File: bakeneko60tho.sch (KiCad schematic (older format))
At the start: 14 parts

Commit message: assign footprints
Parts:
- added D1, D10, D11, D12, D13, D14, D15, D16, D17, D18, D19, D2, D20, D21, D22, D23, D24, D25, D26, D27, D28, D29, D3, D30, D31, D32, D33, D34, D35, D36, D37, D38, D39, D4, D40, D41, D42, D43, D44, D45, D46, D47, D48, D49, D5, D50, D51, D52, D53, D54, D55, D56, D57, D58, D59, D6, D60, D61, D62, D63, D64, D65, D66, D67, D68, D69, D7, D70, D71, D72, D8, D9: SOD-123, Diode_SMD:D_SOD-123, symbol Device:D_Small
- added F1: 500mA, Fuse:Fuse_1206_3216Metric, symbol Device:Polyfuse
- added J1: Conn_01x04_Male, Connector_PinHeader_1.00mm:PinHeader_1x04_P1.00mm_Horizontal, symbol Connector:Conn_01x04_Male
- added MX1, MX10, MX11, MX12, MX13, MX14, MX15, MX16, MX17, MX18, MX19, MX2, MX20, MX21, MX22, MX23, MX24, MX25, MX26, MX27, MX28, MX29, MX3, MX30, MX31, MX32, MX33, MX34, MX35, MX36, MX37, MX38, MX39, MX4, MX40, MX41, MX42, MX44, MX45, MX46, MX47, MX48, MX49, MX5, MX50, MX51, MX52, MX53, MX54, MX55, MX57, MX58, MX59, MX6, MX60, MX61, MX62, MX63, MX65, MX66, MX67, MX68, MX69, MX7, MX70, MX71, MX72, MX8, MX9: MX-NoLED, MX_Only:MXOnly-1U-NoLED, symbol MX_Alps_Hybrid:MX-NoLED
- added MX43, MX56: MX-NoLED, MX_Only:MXOnly-2U-NoLED, symbol MX_Alps_Hybrid:MX-NoLED
- added MX64: MX-NoLED, MX_Only:MXOnly-2U-ReversedStabilizers-NoLED, symbol MX_Alps_Hybrid:MX-NoLED
- C1, C2, C3, C4, C5, C6: renamed from C?; footprint (none) -> Capacitor_SMD:C_0805_2012Metric
- C7: renamed from C?; value 0.1uF -> 10uF; footprint (none) -> Capacitor_SMD:C_0805_2012Metric
- R1, R2, R3, R4: renamed from R?; footprint (none) -> Resistor_SMD:R_0805_2012Metric
- Y1: renamed from Y?; footprint (none) -> Crystal:Crystal_SMD_3225-4Pin_3.2x2.5mm
- gave numbers to parts that had none: 2
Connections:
- net +5V: now also F1.1
- net D+: now also J1.3 (Pin_3)
- net D-: now also J1.2 (Pin_2)
- net GND: now also J1.4 (Pin_4)
- net COL12: now reaches U1.10 (PB2)
- net COL12: now also MX13.1 (COL), MX28.1 (COL), MX43.1 (COL), MX70.1 (COL)
- net COL11: now reaches U1.11 (PB3)
- net COL11: now also MX12.1 (COL), MX27.1 (COL), MX42.1 (COL), MX56.1 (COL), MX69.1 (COL)
- net COL7: now reaches U1.12 (PB7)
- net COL7: now also MX23.1 (COL), MX38.1 (COL), MX52.1 (COL), MX65.1 (COL), MX8.1 (COL)
- net COL6: now reaches U1.18 (PD0)
- net COL6: now also MX22.1 (COL), MX37.1 (COL), MX51.1 (COL), MX7.1 (COL)
- net COL5: now reaches U1.19 (PD1)
- net COL5: now also MX21.1 (COL), MX36.1 (COL), MX50.1 (COL), MX6.1 (COL), MX64.1 (COL)
- net COL4: now reaches U1.20 (PD2)
- net COL4: now also MX20.1 (COL), MX35.1 (COL), MX49.1 (COL), MX5.1 (COL), MX63.1 (COL)
- net COL3: now reaches U1.21 (PD3)
- net COL3: now also MX19.1 (COL), MX34.1 (COL), MX4.1 (COL), MX48.1 (COL), MX62.1 (COL)
- net COL2: now reaches U1.26 (PD6)
- net COL2: now also MX18.1 (COL), MX3.1 (COL), MX33.1 (COL), MX47.1 (COL), MX61.1 (COL)
- net COL1: now reaches U1.27 (PD7)
- net COL1: now also MX17.1 (COL), MX2.1 (COL), MX32.1 (COL), MX46.1 (COL), MX60.1 (COL)
- net COL10: now reaches U1.28 (PB4)
- net COL10: now also MX11.1 (COL), MX26.1 (COL), MX41.1 (COL), MX55.1 (COL), MX68.1 (COL)
- net COL9: now reaches U1.29 (PB5)
- net COL9: now also MX10.1 (COL), MX25.1 (COL), MX40.1 (COL), MX54.1 (COL), MX67.1 (COL)
- net COL8: now reaches U1.30 (PB6)
- net COL8: now also MX24.1 (COL), MX39.1 (COL), MX53.1 (COL), MX66.1 (COL), MX9.1 (COL)
- net ROW4: now reaches U1.36 (PF7)
- net ROW4: now also D59.1 (K), D60.1 (K), D61.1 (K), D62.1 (K), D63.1 (K), D64.1 (K), D65.1 (K), D66.1 (K), D67.1 (K), D68.1 (K), D69.1 (K), D70.1 (K), D71.1 (K), D72.1 (K)
- net ROW3: now reaches U1.37 (PF6)
- net ROW3: now also D45.1 (K), D46.1 (K), D47.1 (K), D48.1 (K), D49.1 (K), D50.1 (K), D51.1 (K), D52.1 (K), D53.1 (K), D54.1 (K), D55.1 (K), D56.1 (K), D57.1 (K), D58.1 (K)
- net ROW2: now reaches U1.38 (PF5)
- net ROW2: now also D31.1 (K), D32.1 (K), D33.1 (K), D34.1 (K), D35.1 (K), D36.1 (K), D37.1 (K), D38.1 (K), D39.1 (K), D40.1 (K), D41.1 (K), D42.1 (K), D43.1 (K), D44.1 (K)
- net ROW1: now reaches U1.39 (PF4)
- net ROW1: now also D16.1 (K), D17.1 (K), D18.1 (K), D19.1 (K), D20.1 (K), D21.1 (K), D22.1 (K), D23.1 (K), D24.1 (K), D25.1 (K), D26.1 (K), D27.1 (K), D28.1 (K), D29.1 (K), D30.1 (K)
- net ROW0: now reaches U1.40 (PF1)
- net ROW0: now also D1.1 (K), D10.1 (K), D11.1 (K), D12.1 (K), D13.1 (K), D14.1 (K), D15.1 (K), D2.1 (K), D3.1 (K), D4.1 (K), D5.1 (K), D6.1 (K), D7.1 (K), D8.1 (K), D9.1 (K)
- net COL0: now reaches U1.41 (PF0)
- net COL0: now also MX1.1 (COL), MX16.1 (COL), MX31.1 (COL), MX45.1 (COL), MX59.1 (COL)
- net COL14: now reaches U1.8 (PB0)
- net COL14: now also MX15.1 (COL), MX30.1 (COL), MX44.1 (COL), MX58.1 (COL), MX72.1 (COL)
- net COL13: now reaches U1.9 (PB1)
- net COL13: now also MX14.1 (COL), MX29.1 (COL), MX57.1 (COL), MX71.1 (COL)
- new net: D36.2 (A), MX36.2 (ROW)
- new net: D37.2 (A), MX37.2 (ROW)
- new net: D38.2 (A), MX38.2 (ROW)
- new net: D39.2 (A), MX39.2 (ROW)
- new net: D40.2 (A), MX40.2 (ROW)
- new net: D41.2 (A), MX41.2 (ROW)
- new net: D42.2 (A), MX42.2 (ROW)
- new net: D43.2 (A), MX43.2 (ROW)
- new net: D44.2 (A), MX44.2 (ROW)
- new net: D31.2 (A), MX31.2 (ROW)
- new net: D32.2 (A), MX32.2 (ROW)
- new net: D33.2 (A), MX33.2 (ROW)
- new net: D34.2 (A), MX34.2 (ROW)
- new net: D35.2 (A), MX35.2 (ROW)
- new net: D50.2 (A), MX50.2 (ROW)
- new net: D51.2 (A), MX51.2 (ROW)
- new net: D52.2 (A), MX52.2 (ROW)
- new net: D53.2 (A), MX53.2 (ROW)
- new net: D54.2 (A), MX54.2 (ROW)
- new net: D55.2 (A), MX55.2 (ROW)
- new net: D56.2 (A), MX56.2 (ROW)
- new net: D57.2 (A), MX57.2 (ROW)
- new net: D58.2 (A), MX58.2 (ROW)
- new net: D45.2 (A), MX45.2 (ROW)
- new net: D46.2 (A), MX46.2 (ROW)
- new net: D47.2 (A), MX47.2 (ROW)
- new net: D48.2 (A), MX48.2 (ROW)
- new net: D49.2 (A), MX49.2 (ROW)
- new net: D64.2 (A), MX64.2 (ROW)
- new net: D65.2 (A), MX65.2 (ROW)
- new net: D66.2 (A), MX66.2 (ROW)
- new net: D67.2 (A), MX67.2 (ROW)
- new net: D68.2 (A), MX68.2 (ROW)
- new net: D69.2 (A), MX69.2 (ROW)
- new net: D70.2 (A), MX70.2 (ROW)
- new net: D71.2 (A), MX71.2 (ROW)
- new net: D72.2 (A), MX72.2 (ROW)
- new net: D59.2 (A), MX59.2 (ROW)
- new net: D60.2 (A), MX60.2 (ROW)
- new net: D61.2 (A), MX61.2 (ROW)
- new net: D62.2 (A), MX62.2 (ROW)
- new net: D63.2 (A), MX63.2 (ROW)
- new net: D6.2 (A), MX6.2 (ROW)
- new net: D7.2 (A), MX7.2 (ROW)
- new net: D8.2 (A), MX8.2 (ROW)
- new net: D9.2 (A), MX9.2 (ROW)
- new net: D10.2 (A), MX10.2 (ROW)
- new net: D11.2 (A), MX11.2 (ROW)
- new net: D12.2 (A), MX12.2 (ROW)
- new net: D13.2 (A), MX13.2 (ROW)
- new net: D14.2 (A), MX14.2 (ROW)
- new net: D15.2 (A), MX15.2 (ROW)
- new net: D1.2 (A), MX1.2 (ROW)
- new net: D2.2 (A), MX2.2 (ROW)
- new net: D3.2 (A), MX3.2 (ROW)
- new net: D4.2 (A), MX4.2 (ROW)
- new net: D5.2 (A), MX5.2 (ROW)
- new net: D21.2 (A), MX21.2 (ROW)
- new net: D22.2 (A), MX22.2 (ROW)
- new net: D23.2 (A), MX23.2 (ROW)
- new net: D24.2 (A), MX24.2 (ROW)
- new net: D25.2 (A), MX25.2 (ROW)
- new net: D26.2 (A), MX26.2 (ROW)
- new net: D27.2 (A), MX27.2 (ROW)
- new net: D28.2 (A), MX28.2 (ROW)
- new net: D29.2 (A), MX29.2 (ROW)
- new net: D30.2 (A), MX30.2 (ROW)
- new net: D16.2 (A), MX16.2 (ROW)
- new net: D17.2 (A), MX17.2 (ROW)
- new net: D18.2 (A), MX18.2 (ROW)
- new net: D19.2 (A), MX19.2 (ROW)
- new net: D20.2 (A), MX20.2 (ROW)
- new net VCC: F1.2, J1.1 (Pin_1)
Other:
- moved on the sheet: C1, C2, C3, C4, C5, C6, C7, R1, R2, R3, R4, SW1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

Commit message: start the pcb
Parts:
- removed U1: ATmega32U4-AU, Package_QFP:TQFP-44_10x10mm_P0.8mm, symbol MCU_Microchip_ATmega:ATmega32U4-AU
- added U?: ATmega32U4-MU, Package_DFN_QFN:QFN-44-1EP_7x7mm_P0.5mm_EP5.2x5.2mm, symbol MCU_Microchip_ATmega:ATmega32U4-MU
- SW1: footprint (none) -> random-keyboard-parts:SKQG-1155865
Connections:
- net +5V: now also U?.14 (VCC), U?.2 (UVCC), U?.24 (AVCC), U?.34 (VCC), U?.44 (AVCC), U?.7 (VBUS)
- net COL0: now also U?.41 (PF0)
- net COL1: now also U?.27 (PD7)
- net COL10: now also U?.28 (PB4)
- net COL11: now also U?.11 (PB3)
- net COL12: now also U?.10 (PB2)
- net COL13: now also U?.9 (PB1)
- net COL14: now also U?.8 (PB0)
- net COL2: now also U?.26 (PD6)
- net COL3: now also U?.21 (PD3)
- net COL4: now also U?.20 (PD2)
- net COL5: now also U?.19 (PD1)
- net COL6: now also U?.18 (PD0)
- net COL7: now also U?.12 (PB7)
- net COL8: now also U?.30 (PB6)
- net COL9: now also U?.29 (PB5)
- net GND: now also U?.15 (GND), U?.23 (GND), U?.35 (GND), U?.43 (GND), U?.45 (GND), U?.5 (UGND)
- net ROW0: now also U?.40 (PF1)
- net ROW1: now also U?.39 (PF4)
- net ROW2: now also U?.38 (PF5)
- net ROW3: now also U?.37 (PF6)
- net ROW4: now also U?.36 (PF7)
- net at R3.1, SW1.2: now also U?.13 (~RESET)
- net at C3.1, Y1.3: now also U?.16 (XTAL2)
- net at C2.1, Y1.1: now also U?.17 (XTAL1)
- net at R1.1: now also U?.3 (D-)
- net at R4.2: now also U?.33 (~HWB~/PE2)
- net at R2.1: now also U?.4 (D+)
- net at C6.1: now also U?.6 (UCAP)
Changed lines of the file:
@@
 EESchema Schematic File Version 4
+LIBS:bakeneko60tho-cache
 EELAYER 30 0
 EELAYER END
@@
 F 0 "SW1" H 7700 1985 50  0000 C CNN
 F 1 "SW_Push" H 7700 1894 50  0000 C CNN
-F 2 "" H 7700 1900 50  0001 C CNN
+F 2 "random-keyboard-parts:SKQG-1155865" H 7700 1900 50  0001 C CNN
 F 3 "~" H 7700 1900 50  0001 C CNN
 	1    7700 1700
 	1    0    0    -1
 $EndComp
-Connection ~ 8600 5000
-Wire Wire Line
-	8600 5000 8700 5000
-Wire Wire Line
-	8250 5000 8600 5000
-Connection ~ 8700 1400
-Connection ~ 8600 1400
-Wire Wire Line
-	8700 1400 8800 1400
-Wire Wire Line
-	8600 1400 8700 1400
 Wire Wire Line
 	7450 2800 8100 2800
-$Comp
-L MCU_Microchip_ATmega:ATmega32U4-AU U1
-U 1 1 627D35F1
-P 8700 3200
-F 0 "U1" H 8700 1311 50  0000 C CNN
-F 1 "ATmega32U4-AU" H 8700 1220 50  0000 C CNN
-F 2 "Package_QFP:TQFP-44_10x10mm_P0.8mm" H 8700 3200 50  0001 C CIN
-F 3 "http://ww1.microchip.com/downloads/en/DeviceDoc/Atmel-7766-8-bit-AVR-ATmega16U4-32U4_Datasheet.pdf" H 8700 3200 50  0001 C CNN
-	1    8700 3200
-	1    0    0    -1
-$EndComp
 Wire Wire Line
 	7900 1700 8000 1700
@@
 Wire Wire Line
 	9300 4600 9550 4600
+Wire Wire Line
+	8600 1400 8700 1400
+Wire Wire Line
+	8250 5000 8600 5000
+$Comp
+L MCU_Microchip_ATmega:ATmega32U4-MU U?
+U 1 1 62ABC593
+P 8700 3200
+F 0 "U?" H 8700 1311 50  0000 C CNN
+F 1 "ATmega32U4-MU" H 8700 1220 50  0000 C CNN
+F 2 "Package_DFN_QFN:QFN-44-1EP_7x7mm_P0.5mm_EP5.2x5.2mm" H 8700 3200 50  0001 C CIN
+F 3 "http://ww1.microchip.com/downloads/en/DeviceDoc/Atmel-7766-8-bit-AVR-ATmega16U4-32U4_Datasheet.pdf" H 8700 3200 50  0001 C CNN
+	1    8700 3200
+	1    0    0    -1
+$EndComp
+Connection ~ 8600 1400
+Wire Wire Line
+	8600 5000 8700 5000
+Connection ~ 8600 5000
+Wire Wire Line
+	8700 1400 8800 1400
+Connection ~ 8700 1400
 $EndSCHEMATC

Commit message: complete routing
finishing the routing
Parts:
- removed U?: ATmega32U4-MU, Package_DFN_QFN:QFN-44-1EP_7x7mm_P0.5mm_EP5.2x5.2mm, symbol MCU_Microchip_ATmega:ATmega32U4-MU
- added U1: ATmega32U4-AU, Package_QFP:TQFP-44_10x10mm_P0.8mm, symbol MCU_Microchip_ATmega:ATmega32U4-AU
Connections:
- net +5V: now also F1.2, U1.14 (VCC), U1.2 (UVCC), U1.24 (AVCC), U1.34 (VCC), U1.44 (AVCC), U1.7 (VBUS); no longer F1.1
- net COL0: now also U1.36 (PF7)
- net COL1: now also U1.37 (PF6)
- net COL10: now also U1.12 (PB7)
- net COL11: now also U1.21 (PD3)
- net COL12: now also U1.20 (PD2)
- net COL13: now also U1.19 (PD1)
- net COL14: now also U1.18 (PD0)
- net COL2: now also U1.38 (PF5)
- net COL3: now also U1.39 (PF4)
- net COL4: now also U1.40 (PF1)
- net COL5: now also U1.41 (PF0)
- net COL6: now also U1.8 (PB0)
- net COL7: now also U1.9 (PB1)
- net COL8: now also U1.10 (PB2)
- net COL9: now also U1.11 (PB3)
- net D+: now also J1.2 (Pin_2); no longer J1.3 (Pin_3)
- net D-: now also J1.3 (Pin_3); no longer J1.2 (Pin_2)
- net GND: now also J1.1 (Pin_1), U1.15 (GND), U1.23 (GND), U1.35 (GND), U1.43 (GND), U1.5 (UGND); no longer J1.4 (Pin_4)
- net ROW0: now also U1.27 (PD7)
- net ROW1: now also U1.26 (PD6)
- net ROW2: now also U1.30 (PB6)
- net ROW3: now also U1.29 (PB5)
- net ROW4: now also U1.28 (PB4)
- net VCC: now also F1.1, J1.4 (Pin_4); no longer F1.2, J1.1 (Pin_1)
- net at R4.2: now also U1.33 (~HWB~/PE2)
- net at R2.1: now also U1.4 (D+)
- net at R1.1: now also U1.3 (D-)
- net at C6.1: now also U1.6 (UCAP)
- net at C2.1, Y1.1: now also U1.17 (XTAL1)
- net at C3.1, Y1.3: now also U1.16 (XTAL2)
- net at R3.1, SW1.2: now also U1.13 (~RESET)
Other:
- moved on the sheet: F1, J1

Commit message: fix routing
fix routing bugs
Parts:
- removed J1: Conn_01x04_Male, Connector_PinHeader_1.00mm:PinHeader_1x04_P1.00mm_Horizontal, symbol Connector:Conn_01x04_Male
- added J1: GND, Connector_PinHeader_1.00mm:PinHeader_1x01_P1.00mm_Vertical, symbol Connector:Conn_01x01_Male
- added J2: D+, Connector_PinHeader_1.00mm:PinHeader_1x01_P1.00mm_Vertical, symbol Connector:Conn_01x01_Male
- added J3: D-, Connector_PinHeader_1.00mm:PinHeader_1x01_P1.00mm_Vertical, symbol Connector:Conn_01x01_Male
- added J4: vcc, Connector_PinHeader_1.00mm:PinHeader_1x01_P1.00mm_Vertical, symbol Connector:Conn_01x01_Male
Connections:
- net D+: now also J2.1 (Pin_1)
- net D-: now also J3.1 (Pin_1)
- net GND: now also J1.1 (Pin_1)
- net VCC: now also J4.1 (Pin_1)
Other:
- moved on the sheet: F1
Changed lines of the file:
@@
 L power:+5V #PWR0111
 U 1 1 62850546
-P 6550 4750
-F 0 "#PWR0111" H 6550 4600 50  0001 C CNN
-F 1 "+5V" H 6565 4923 50  0000 C CNN
-F 2 "" H 6550 4750 50  0001 C CNN
-F 3 "" H 6550 4750 50  0001 C CNN
-	1    6550 4750
+P 7500 5100
+F 0 "#PWR0111" H 7500 4950 50  0001 C CNN
+F 1 "+5V" H 7515 5273 50  0000 C CNN
+F 2 "" H 7500 5100 50  0001 C CNN
+F 3 "" H 7500 5100 50  0001 C CNN
+	1    7500 5100
 	1    0    0    -1
 $EndComp
@@
 L Device:Polyfuse F1
 U 1 1 6284E1C3
-P 6900 4750
-F 0 "F1" V 6675 4750 50  0000 C CNN
-F 1 "500mA" V 6766 4750 50  0000 C CNN
-F 2 "Fuse:Fuse_1206_3216Metric" H 6950 4550 50  0001 L CNN
-F 3 "~" H 6900 4750 50  0001 C CNN
-	1    6900 4750
-	0    1    1    0
+P 7150 5100
+F 0 "F1" V 6925 5100 50  0000 C CNN
+F 1 "500mA" V 7016 5100 50  0000 C CNN
+F 2 "Fuse:Fuse_1206_3216Metric" H 7200 4900 50  0001 L CNN
+F 3 "~" H 7150 5100 50  0001 C CNN
+	1    7150 5100
+	0    -1   -1   0
 $EndComp
 $Comp
 L power:VCC #PWR0112
 U 1 1 6284D4F2
-P 7250 4750
-F 0 "#PWR0112" H 7250 4600 50  0001 C CNN
-F 1 "VCC" H 7267 4923 50  0000 C CNN
-F 2 "" H 7250 4750 50  0001 C CNN
-F 3 "" H 7250 4750 50  0001 C CNN
-	1    7250 4750
-	1    0    0    -1
-$EndComp
-$Comp
-L Connector:Conn_01x04_Male J1
-U 1 1 6288D02A
-P 7650 4950
-F 0 "J1" H 7758 5231 50  0000 C CNN
-F 1 "Conn_01x04_Male" H 7758 5140 50  0000 C CNN
-F 2 "Connector_PinHeader_1.00mm:PinHeader_1x04_P1.00mm_Horizontal" H 7650 4950 50  0001 C CNN
-F 3 "~" H 7650 4950 50  0001 C CNN
-	1    7650 4950
-	-1   0    0    1
-$EndComp
-Text GLabel 7250 4950 0    50   Input ~ 0
-D+
-Text GLabel 7250 4850 0    50   Input ~ 0
-D-
+P 6800 5100
+F 0 "#PWR0112" H 6800 4950 50  0001 C CNN
+F 1 "VCC" H 6817 5273 50  0000 C CNN
+F 2 "" H 6800 5100 50  0001 C CNN
+F 3 "" H 6800 5100 50  0001 C CNN
+	1    6800 5100
+	1    0    0    -1
+$EndComp
 $Comp
 L power:GND #PWR0113
 U 1 1 628948D3
-P 7150 5050
-F 0 "#PWR0113" H 7150 4800 50  0001 C CNN
-F 1 "GND" H 7155 4877 50  0000 C CNN
-F 2 "" H 7150 5050 50  0001 C CNN
-F 3 "" H 7150 5050 50  0001 C CNN
-	1    7150 5050
+P 6900 5850
+F 0 "#PWR0113" H 6900 5600 50  0001 C CNN
+F 1 "GND" H 6905 5677 50  0000 C CNN
+F 2 "" H 6900 5850 50  0001 C CNN
+F 3 "" H 6900 5850 50  0001 C CNN
+	1    6900 5850
 	1    0    0    -1
 $EndComp
@@
 ROW0
 Wire Wire Line
-	7150 5050 7450 5050
-Wire Wire Line
-	7250 4950 7450 4950
-Wire Wire Line
-	7250 4850 7450 4850
-Wire Wire Line
-	6550 4750 6750 4750
-Wire Wire Line
-	7050 4750 7250 4750
-Wire Wire Line
-	7250 4750 7450 4750
-Connection ~ 7250 4750
+	6900 5850 6600 5850
+Wire Wire Line
+	7500 5100 7300 5100
+Wire Wire Line
+	7000 5100 6800 5100
+Wire Wire Line
+	6800 5100 6600 5100
+Connection ~ 6800 5100
 Wire Wire Line
 	8600 1400 8700 1400
@@
 Wire Wire Line
 	9300 4600 9550 4600
+$Comp
+L Connector:Conn_01x01_Male J4
+U 1 1 62DF2DF2
+P 6400 5100
+F 0 "J4" H 6508 5281 50  0000 C CNN
+F 1 "vcc" H 6508 5190 50  0000 C CNN
+F 2 "Connector_PinHeader_1.00mm:PinHeader_1x01_P1.00mm_Vertical" H 6400 5100 50  0001 C CNN
+F 3 "~" H 6400 5100 50  0001 C CNN
+	1    6400 5100
+	1    0    0    -1
+$EndComp
+$Comp
+L Connector:Conn_01x01_Male J1
+U 1 1 62DF4B11
+P 6400 5850
+F 0 "J1" H 6508 6031 50  0000 C CNN
+F 1 "GND" H 6508 5940 50  0000 C CNN
+F 2 "Connector_PinHeader_1.00mm:PinHeader_1x01_P1.00mm_Vertical" H 6400 5850 50  0001 C CNN
+F 3 "~" H 6400 5850 50  0001 C CNN
+	1    6400 5850
+	1    0    0    -1
+$EndComp
+$Comp
+L Connector:Conn_01x01_Male J3
+U 1 1 62DF471A
+P 6400 5350
+F 0 "J3" H 6508 5531 50  0000 C CNN
+F 1 "D-" H 6508 5440 50  0000 C CNN
+F 2 "Connector_PinHeader_1.00mm:PinHeader_1x01_P1.00mm_Vertical" H 6400 5350 50  0001 C CNN
+F 3 "~" H 6400 5350 50  0001 C CNN
+	1    6400 5350
+	1    0    0    -1
+$EndComp
+Wire Wire Line
+	6600 5350 6800 5350
+Text GLabel 6800 5350 2    50   Input ~ 0
+D-
+$Comp
+L Connector:Conn_01x01_Male J2
+U 1 1 62DF4913
+P 6400 5600
+F 0 "J2" H 6508 5781 50  0000 C CNN
+F 1 "D+" H 6508 5690 50  0000 C CNN
+F 2 "Connector_PinHeader_1.00mm:PinHeader_1x01_P1.00mm_Vertical" H 6400 5600 50  0001 C CNN
+F 3 "~" H 6400 5600 50  0001 C CNN
+	1    6400 5600
+	1    0    0    -1
+$EndComp
+Wire Wire Line
+	6800 5600 6600 5600
+Text GLabel 6800 5600 2    50   Input ~ 0
+D+
 $EndSCHEMATC

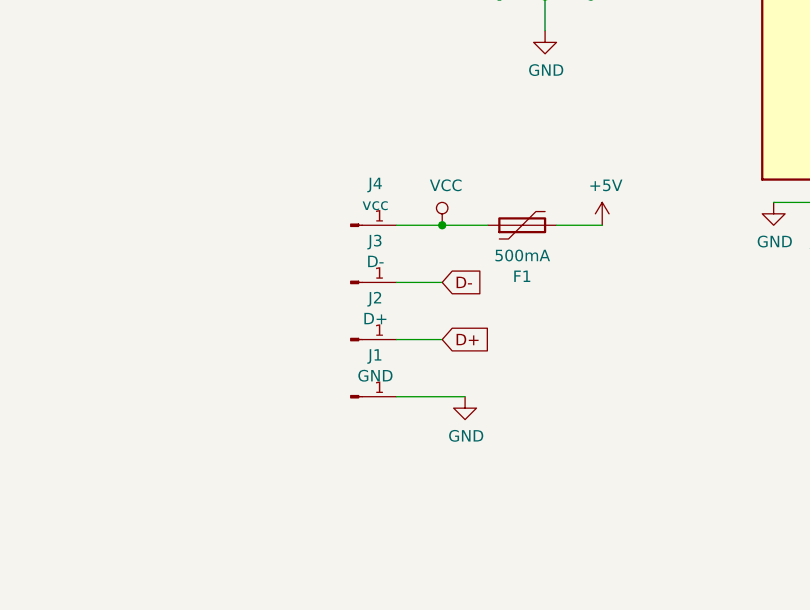
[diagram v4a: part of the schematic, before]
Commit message: use jst for usb conn
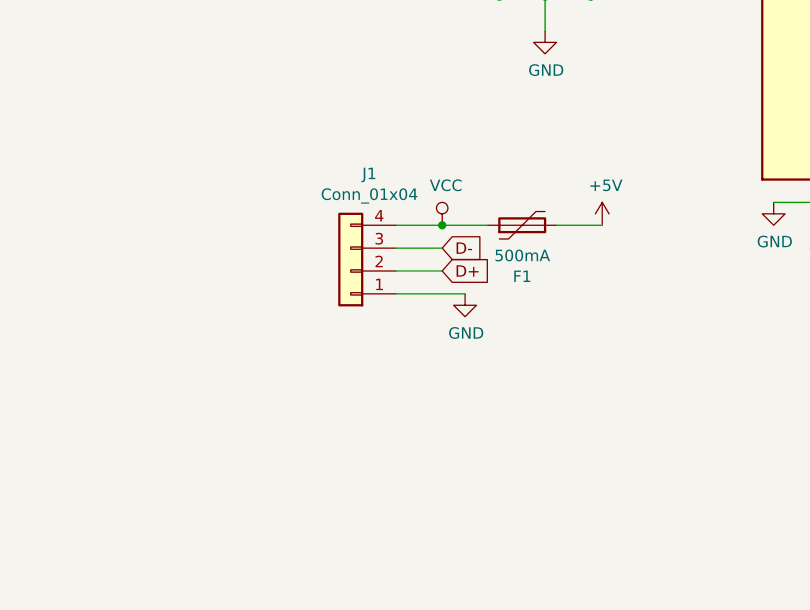
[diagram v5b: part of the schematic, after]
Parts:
- removed J1: GND, Connector_PinHeader_1.00mm:PinHeader_1x01_P1.00mm_Vertical, symbol Connector:Conn_01x01_Male
- removed J2: D+, Connector_PinHeader_1.00mm:PinHeader_1x01_P1.00mm_Vertical, symbol Connector:Conn_01x01_Male
- removed J3: D-, Connector_PinHeader_1.00mm:PinHeader_1x01_P1.00mm_Vertical, symbol Connector:Conn_01x01_Male
- removed J4: vcc, Connector_PinHeader_1.00mm:PinHeader_1x01_P1.00mm_Vertical, symbol Connector:Conn_01x01_Male
- added J1: Conn_01x04, Connector_JST:JST_SH_SM04B-SRSS-TB_1x04-1MP_P1.00mm_Horizontal, symbol Connector_Generic:Conn_01x04
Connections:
- net D+: now also J1.2 (Pin_2)
- net D-: now also J1.3 (Pin_3)
- net GND: now also J1.1 (Pin_1)
- net VCC: now also J1.4 (Pin_4)
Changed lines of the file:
@@
-	1    0    0    -1
-$EndComp
-$Comp
-L power:GND #PWR0113
-U 1 1 628948D3
-P 6900 5850
-F 0 "#PWR0113" H 6900 5600 50  0001 C CNN
-F 1 "GND" H 6905 5677 50  0000 C CNN
-F 2 "" H 6900 5850 50  0001 C CNN
-F 3 "" H 6900 5850 50  0001 C CNN
-	1    6900 5850
 	1    0    0    -1
 $EndComp
@@
 ROW0
 Wire Wire Line
-	6900 5850 6600 5850
-Wire Wire Line
 	7500 5100 7300 5100
 Wire Wire Line
 	7000 5100 6800 5100
-Wire Wire Line
-	6800 5100 6600 5100
 Connection ~ 6800 5100
 Wire Wire Line
@@
 Wire Wire Line
 	9300 4600 9550 4600
-$Comp
-L Connector:Conn_01x01_Male J4
-U 1 1 62DF2DF2
-P 6400 5100
-F 0 "J4" H 6508 5281 50  0000 C CNN
-F 1 "vcc" H 6508 5190 50  0000 C CNN
-F 2 "Connector_PinHeader_1.00mm:PinHeader_1x01_P1.00mm_Vertical" H 6400 5100 50  0001 C CNN
-F 3 "~" H 6400 5100 50  0001 C CNN
-	1    6400 5100
-	1    0    0    -1
-$EndComp
-$Comp
-L Connector:Conn_01x01_Male J1
-U 1 1 62DF4B11
-P 6400 5850
-F 0 "J1" H 6508 6031 50  0000 C CNN
-F 1 "GND" H 6508 5940 50  0000 C CNN
-F 2 "Connector_PinHeader_1.00mm:PinHeader_1x01_P1.00mm_Vertical" H 6400 5850 50  0001 C CNN
-F 3 "~" H 6400 5850 50  0001 C CNN
-	1    6400 5850
-	1    0    0    -1
-$EndComp
-$Comp
-L Connector:Conn_01x01_Male J3
-U 1 1 62DF471A
-P 6400 5350
-F 0 "J3" H 6508 5531 50  0000 C CNN
-F 1 "D-" H 6508 5440 50  0000 C CNN
-F 2 "Connector_PinHeader_1.00mm:PinHeader_1x01_P1.00mm_Vertical" H 6400 5350 50  0001 C CNN
-F 3 "~" H 6400 5350 50  0001 C CNN
-	1    6400 5350
-	1    0    0    -1
-$EndComp
-Wire Wire Line
-	6600 5350 6800 5350
-Text GLabel 6800 5350 2    50   Input ~ 0
+Text GLabel 6800 5300 2    50   Input ~ 0
+D+
+Wire Wire Line
+	6800 5300 6600 5300
+Text GLabel 6800 5200 2    50   Input ~ 0
 D-
-$Comp
-L Connector:Conn_01x01_Male J2
-U 1 1 62DF4913
-P 6400 5600
-F 0 "J2" H 6508 5781 50  0000 C CNN
-F 1 "D+" H 6508 5690 50  0000 C CNN
-F 2 "Connector_PinHeader_1.00mm:PinHeader_1x01_P1.00mm_Vertical" H 6400 5600 50  0001 C CNN
-F 3 "~" H 6400 5600 50  0001 C CNN
-	1    6400 5600
-	1    0    0    -1
-$EndComp
-Wire Wire Line
-	6800 5600 6600 5600
-Text GLabel 6800 5600 2    50   Input ~ 0
-D+
+Wire Wire Line
+	6600 5200 6800 5200
+Wire Wire Line
+	6800 5100 6600 5100
+$Comp
+L Connector_Generic:Conn_01x04 J1
+U 1 1 63177917
+P 6400 5300
+F 0 "J1" H 6318 4875 50  0000 C CNN
+F 1 "Conn_01x04" H 6318 4966 50  0000 C CNN
+F 2 "Connector_JST:JST_SH_SM04B-SRSS-TB_1x04-1MP_P1.00mm_Horizontal" H 6400 5300 50  0001 C CNN
+F 3 "~" H 6400 5300 50  0001 C CNN
+	1    6400 5300
+	-1   0    0    1
+$EndComp
+Wire Wire Line
+	6900 5400 6600 5400
+$Comp
+L power:GND #PWR0113
+U 1 1 628948D3
+P 6900 5400
+F 0 "#PWR0113" H 6900 5150 50  0001 C CNN
+F 1 "GND" H 6905 5227 50  0000 C CNN
+F 2 "" H 6900 5400 50  0001 C CNN
+F 3 "" H 6900 5400 50  0001 C CNN
+	1    6900 5400
+	1    0    0    -1
+$EndComp
 $EndSCHEMATC
